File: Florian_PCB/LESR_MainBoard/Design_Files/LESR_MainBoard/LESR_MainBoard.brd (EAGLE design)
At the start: 73.8 x 38.4 mm, 46 parts, among them Q1 SS8050-G, Q2 SS8050-G, U1 TCA9548APWR, U2 NCP1117ST33T3G, U3 ESP32-WROOM-32, U4 CP2102N-A01-GQFN28, U5 SP0503BAHT

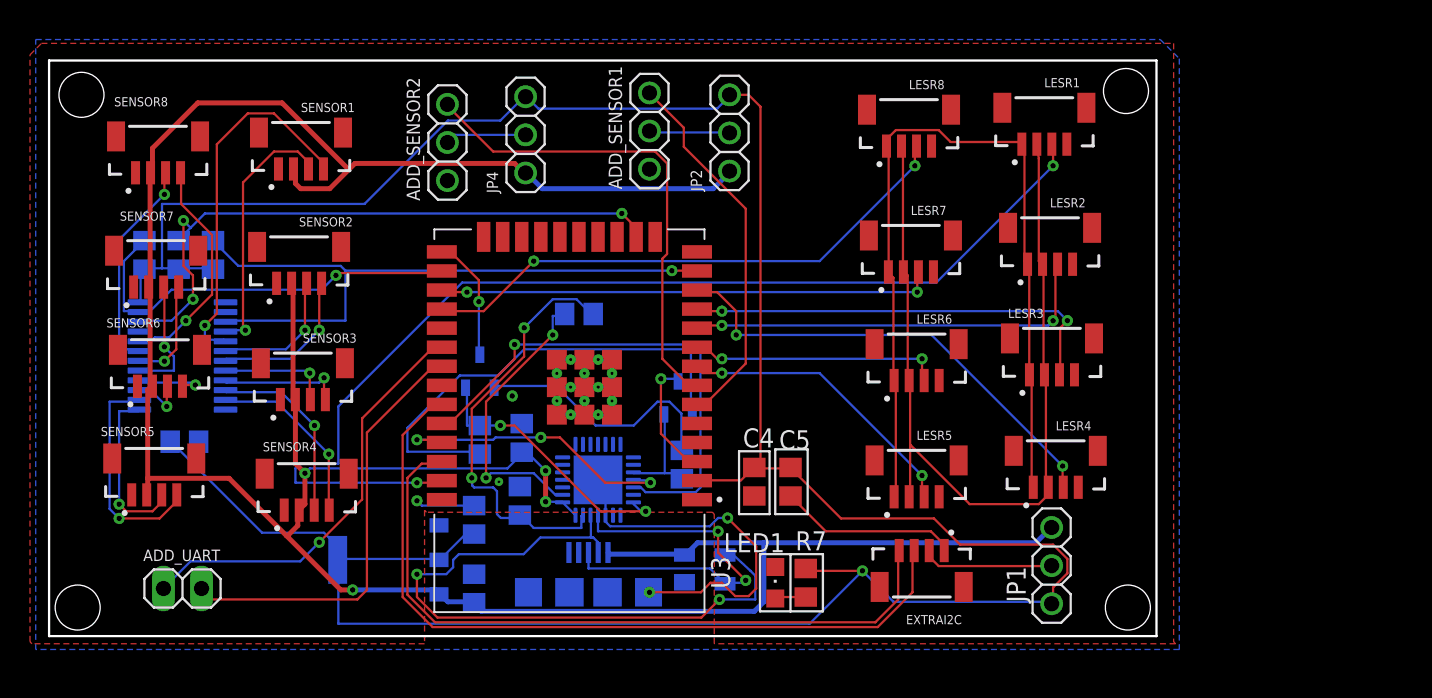
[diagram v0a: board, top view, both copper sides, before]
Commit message: JST Updated in Main B
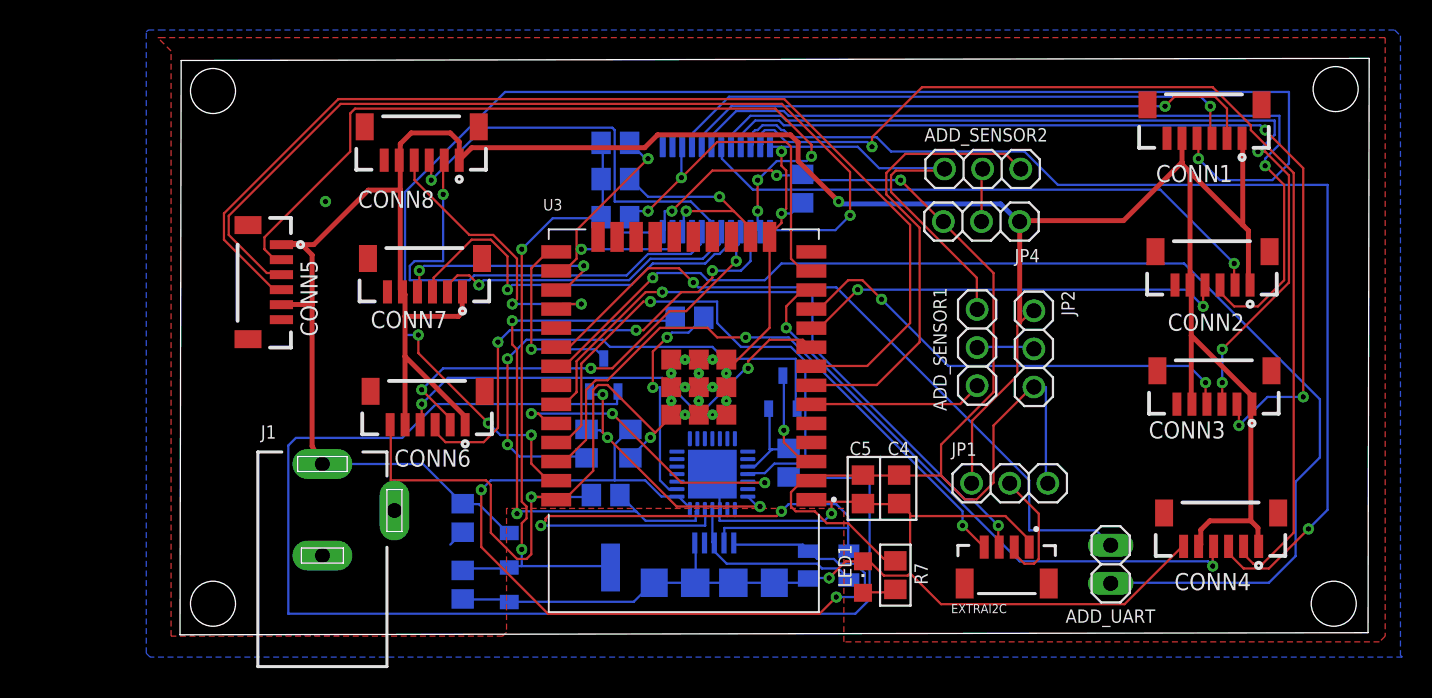
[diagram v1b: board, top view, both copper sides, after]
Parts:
- removed LESR1, LESR2, LESR3, LESR4, LESR5, LESR6, LESR7, LESR8, SENSOR1, SENSOR2, SENSOR3, SENSOR4, SENSOR5, SENSOR6, SENSOR7, SENSOR8: Vertical Qwiic Connector, SparkFun-Connectors:JST04_1MM_VERT
- added CONN1, CONN2, CONN3, CONN4, CONN5, CONN6, CONN7, CONN8: JST_6_PIN_VERTICAL, SparkFun-Connectors:JST-6-SMD-VERT-1.0MM
- added J1: DCJ0202, con-jack:DCJ0202
- moved ADD_UART 61.9 mm to (83.1, 4.41), turned to 270 degrees
- moved C3 44.5 mm to (62.5, 29.4), turned to 270 degrees
- moved U1 37.3 mm to (56.8, 29.4), turned to 270 degrees
- moved ADD_SENSOR2 35.7 mm to (74.5, 30.7), turned to 0 degrees
- moved R3 32.3 mm to (50.1, 32.5), turned to 0 degrees
- moved JP4 30.9 mm to (74.4, 27.2), turned to 180 degrees
- moved R2 29.5 mm to (50.1, 30.1), turned to 0 degrees
- moved R1 26.9 mm to (50.1, 27.5), turned to 0 degrees
- moved ADD_SENSOR1 26.2 mm to (74.2, 18.8), turned to 270 degrees
- moved JP2 24.9 mm to (77.9, 18.8), turned to 270 degrees
- moved U2 11.4 mm to (46.4, 4.19), turned to 90 degrees
- moved C4 9.67 mm to (69.0, 9.40)
- moved USB 8.41 mm to (56.6, 3.17)
- moved Q1 8.26 mm to (49.3, 17.0)
- moved U5 8.26 mm to (64.3, 4.32)
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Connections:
- removed net 1: LESR1.1, LESR2.1, LESR3.1, LESR4.1, LESR5.1, LESR6.1, LESR7.1, LESR8.1
- removed net 2: LESR1.2, LESR2.2, LESR3.2, LESR4.2, LESR5.2, LESR6.2, LESR7.2, LESR8.2
- new net VIN: C1.1, CONN1.1, CONN1.5, CONN2.1, CONN2.5, CONN3.1, CONN3.5, CONN4.1, CONN4.5, CONN5.1, CONN5.5, CONN6.1, CONN6.5, CONN7.1, CONN7.5, CONN8.1, CONN8.5, J1.1, JP1.1, JP2.1, JP4.1, U2.3
- net GND: now also CONN1.6, CONN2.6, CONN3.6, CONN4.6, CONN5.6, CONN6.6, CONN7.6, CONN8.6, J1.2, J1.3; no longer SENSOR1.1, SENSOR2.1, SENSOR3.1, SENSOR4.1, SENSOR5.1, SENSOR6.1, SENSOR7.1, SENSOR8.1
- net IO16: now also CONN7.4; no longer LESR7.3
- net IO17: now also CONN8.4; no longer LESR8.3
- net IO23: now also CONN1.4; no longer LESR1.3
- net IO25: now also CONN2.4; no longer LESR2.3
- net IO26: now also CONN3.4; no longer LESR3.3
- net IO27: now also CONN4.4; no longer LESR4.3
- net IO32: now also CONN5.4; no longer LESR5.3
- net IO33: now also CONN6.4; no longer LESR6.3
- net SC0: now also CONN1.2; no longer SENSOR1.4
- net SC1: now also CONN2.2; no longer SENSOR2.4
- net SC2: now also CONN3.2; no longer SENSOR3.4
- net SC3: now also CONN4.2; no longer SENSOR4.4
- net SC4: now also CONN5.2; no longer SENSOR5.4
- net SC5: now also CONN6.2; no longer SENSOR6.4
- net SC6: now also CONN7.2; no longer SENSOR7.4
- net SC7: now also CONN8.2; no longer SENSOR8.4
- net SD0: now also CONN1.3; no longer SENSOR1.3
- net SD1: now also CONN2.3; no longer SENSOR2.3
- net SD2: now also CONN3.3; no longer SENSOR3.3
- net SD3: now also CONN4.3; no longer SENSOR4.3
- net SD4: now also CONN5.3; no longer SENSOR5.3
- net SD5: now also CONN6.3; no longer SENSOR6.3
- net SD6: now also CONN7.3; no longer SENSOR7.3
- net SD7: now also CONN8.3; no longer SENSOR8.3
- net VBUS: no longer C1.1, JP1.1, JP2.1, JP4.1, SENSOR1.2, SENSOR2.2, SENSOR3.2, SENSOR4.2, SENSOR5.2, SENSOR6.2, SENSOR7.2, SENSOR8.2, U2.3
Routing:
- net VIN: track 0.00 -> 206.0 mm, vias 0 -> 1
- net GND: track 41.3 -> 199.9 mm, vias 5 -> 7
- net VBUS: track 190.6 -> 61.9 mm, vias 4 -> 2
- net N$3: track 17.1 -> 87.8 mm
- net 3.3V: track 193.5 -> 129.0 mm, vias 1 -> 5
- net SD3: track 12.6 -> 71.8 mm
- net 2: track 58.5 -> 0.00 mm
- net SC3: track 12.1 -> 70.4 mm
- net 1: track 57.1 -> 0.00 mm
- net IO32: track 19.5 -> 73.7 mm, vias 2 -> 0
- net SC2: track 8.33 -> 61.7 mm, vias 1 -> 3
- net E_RX: track 28.9 -> 82.0 mm, vias 0 -> 1
- net SD2: track 7.47 -> 59.9 mm, vias 1 -> 3
- net SD4: track 11.4 -> 61.0 mm
- net SD1: track 9.06 -> 57.0 mm
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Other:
- board size 73.8 x 38.4 mm -> 79.2 x 38.4 mm
